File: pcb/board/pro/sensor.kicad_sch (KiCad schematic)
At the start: 1 part, among them U1 AH49HSC

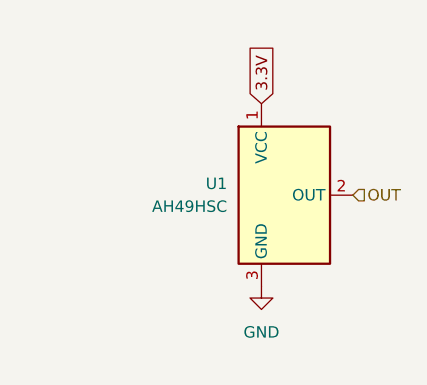
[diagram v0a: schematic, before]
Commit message: Updated with filter caps
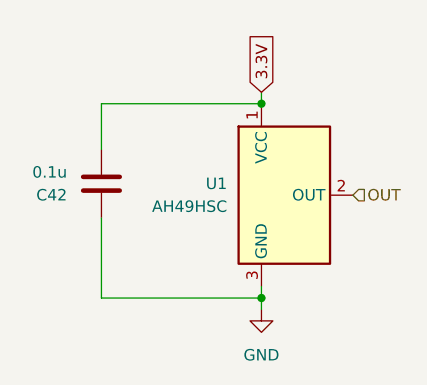
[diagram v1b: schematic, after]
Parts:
- added C42: 0.1u, Capacitor_SMD:C_0402_1005Metric, symbol Device:C
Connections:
- net 3.3V: now also C42.2
- net GND: now also C42.1
